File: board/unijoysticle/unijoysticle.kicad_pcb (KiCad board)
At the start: 2 copper layers, 57.9 x 52.6 mm, 10 parts, among them J1 DB9_Female_MountingHoles, J2 DB9_Female_MountingHoles, J3 Barrel_Jack_MountingPin, SW1 SW_SPDT, U1 4066, U2 4066, U4 4066, U5 4066

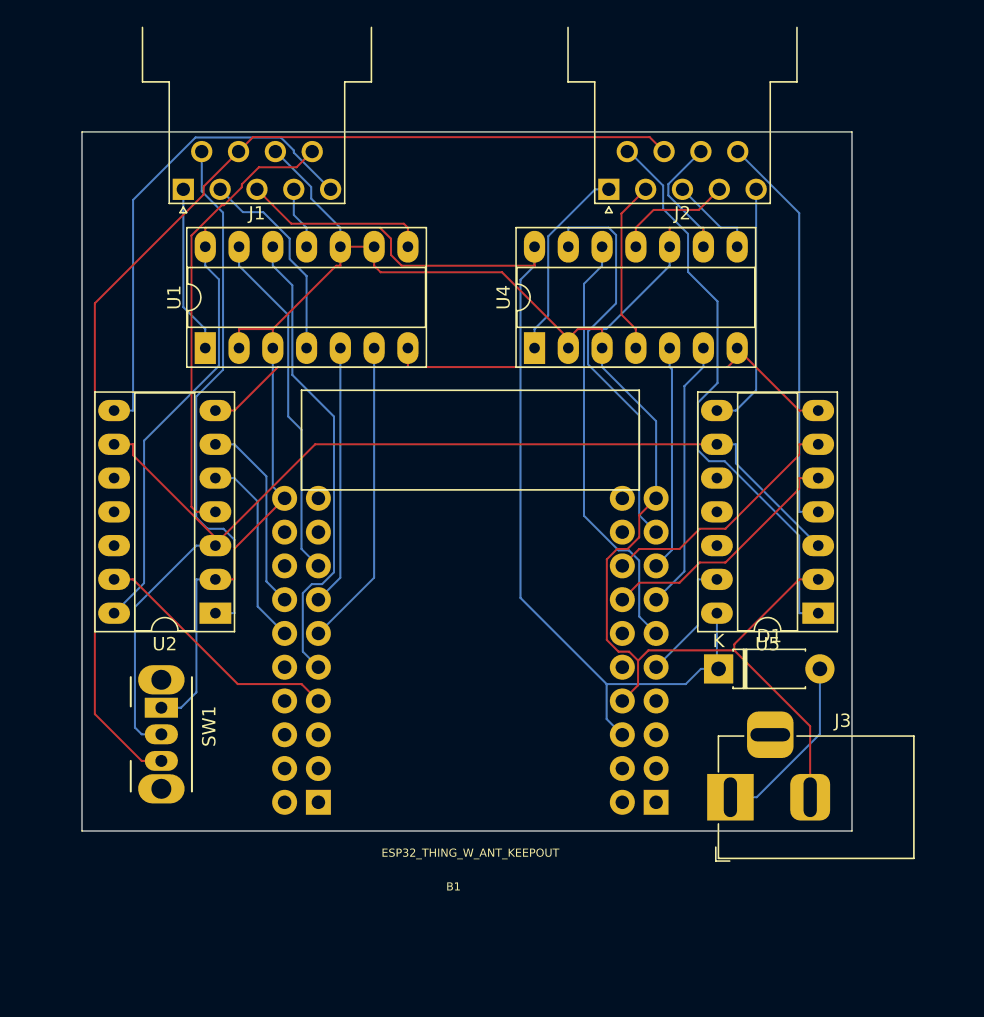
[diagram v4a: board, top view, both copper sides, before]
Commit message: board: using new db9 female to avoid errors.
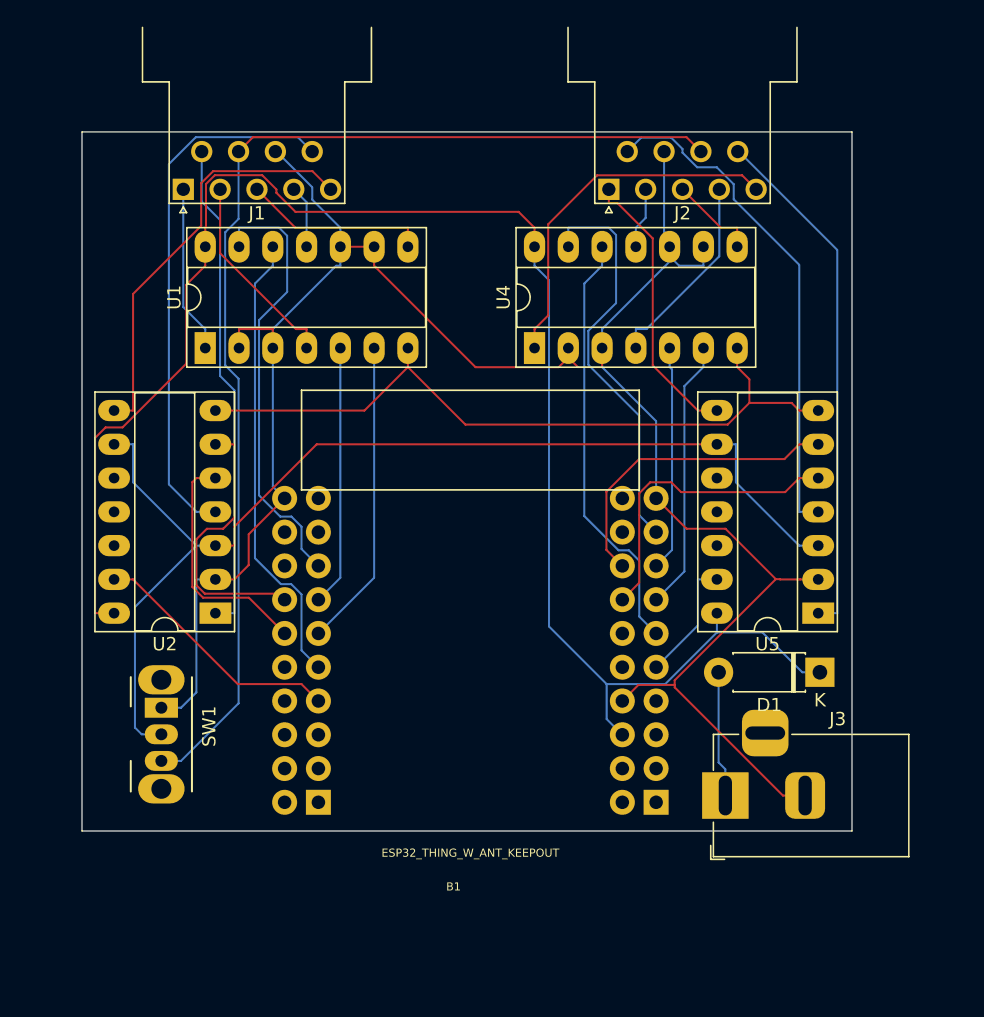
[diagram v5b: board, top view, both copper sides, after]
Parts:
- J1, J2: value DB9_Female_MountingHoles -> DB9_Female
- J3: value Barrel_Jack_MountingPin -> Barrel_Jack
- moved D1 7.62 mm to (168.7, 115.6), turned to 180 degrees
- moved J3 0.40 mm to (161.5, 124.8)
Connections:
- J2 pad 1: J2UP -> J2POTY
- J2 pad 2: J2DOWN -> J2RIGHT
- J2 pad 4: J2RIGHT -> J2DOWN
- J2 pad 5: J2POTY -> J2UP
- J2 pad 6: J2FIRE -> J2POTX
- J2 pad 7: J1POWER -> GND
- J2 pad 8: GND -> J1POWER
- J2 pad 9: J2POTX -> J2FIRE
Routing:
- net J2UP: track 14.9 -> 27.3 mm
- net Vdd: track 114.4 -> 125.9 mm
- net J2POTX: track 30.4 -> 38.2 mm
- net GPIO_J1UP: track 26.5 -> 33.3 mm
- net GPIO_J1POTY: track 14.7 -> 21.0 mm
- net J1POTX: track 34.2 -> 40.5 mm
- net GND: track 169.3 -> 163.2 mm
- net Vss: track 50.8 -> 55.3 mm
- net GPIO_J2POTY: track 19.0 -> 23.5 mm
- net J1POTY: track 35.8 -> 31.3 mm
- net J2RIGHT: track 8.90 -> 4.62 mm
- net J2FIRE: track 43.5 -> 39.3 mm
- net Net-(D1-Pad2): track 13.6 -> 9.48 mm
- net GPIO_J2POTX: track 19.0 -> 23.1 mm
- net GPIO_J1POTX: track 14.7 -> 18.1 mm
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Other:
- rule via_min_drill: 0.254 -> 0.3302
- rule via_min_size: 0.508 -> 0.6858

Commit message: board: add logo in back silkscreen
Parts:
- added G***: LOGO, Parts:unijoysticle_logo, B.Cu at (141.5, 106.4)
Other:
- board text added: "Unijoysticle 2 v0.0.1 http://retro.moe"

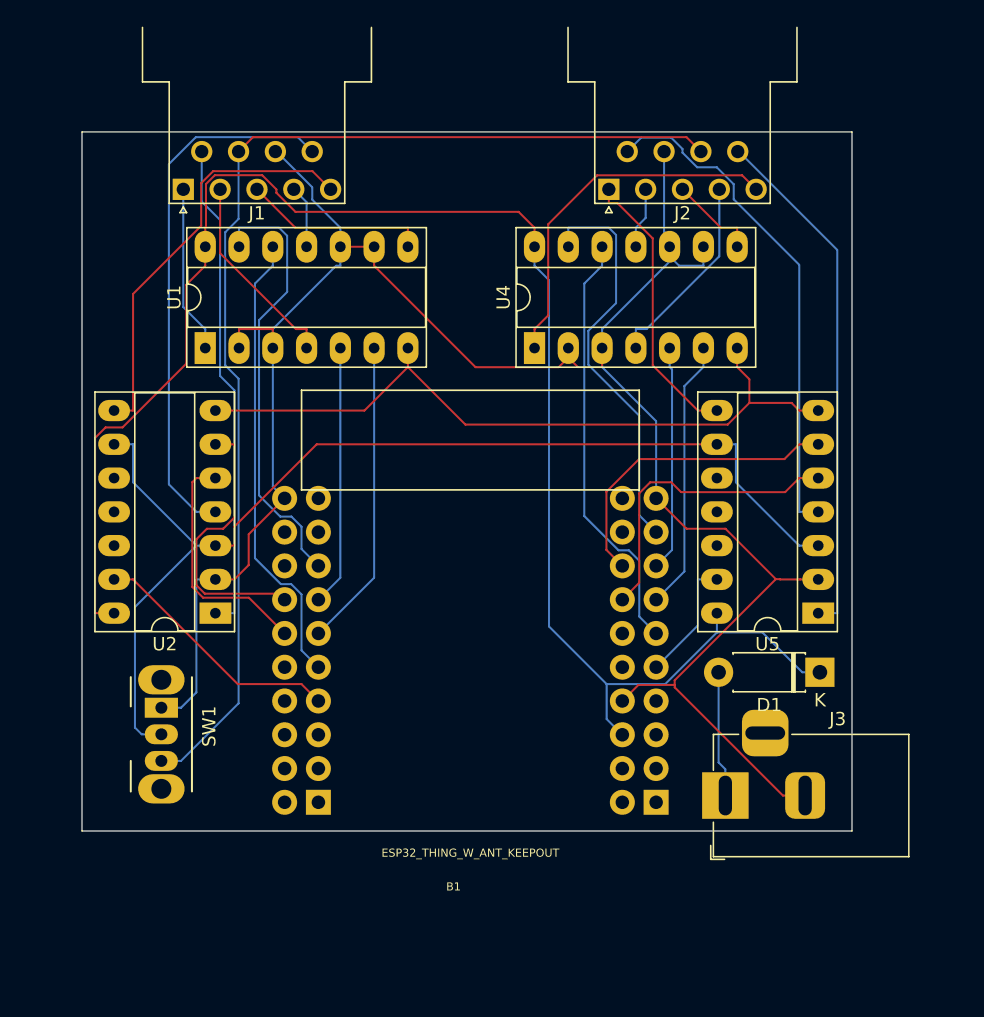
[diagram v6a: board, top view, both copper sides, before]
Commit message: board: autorouting ok. j1 & j2 connected correctly
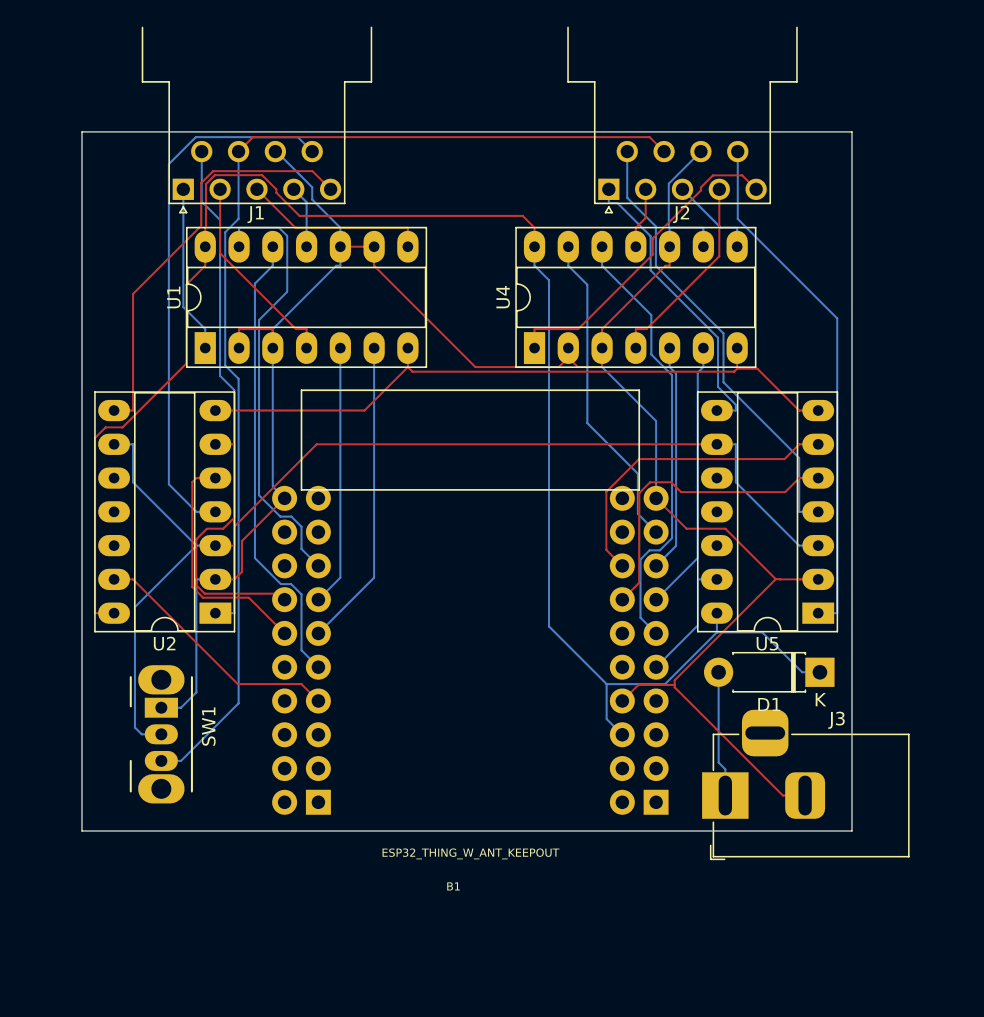
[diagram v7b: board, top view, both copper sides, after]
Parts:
- removed G***: LOGO, Parts:unijoysticle_logo
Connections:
- B1 pad 2: VDD -> Vdd
- D1 pad 1: VDD -> Vdd
- J2 pad 7: GND -> J1POWER
- J2 pad 8: J1POWER -> GND
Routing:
- net GPIO_J2UP: track 30.6 -> 24.2 mm
- net J2POTX: track 38.2 -> 33.9 mm
- net Vss: track 55.3 -> 51.2 mm
- net J2UP: track 27.3 -> 24.2 mm
- net J1POWER: track 85.6 -> 82.8 mm
- net J2POTY: track 21.2 -> 22.4 mm
- net GPIO_J2RIGHT: track 32.3 -> 33.2 mm
- net GND: track 163.2 -> 164.0 mm

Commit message: board: logo re-added, c64/amiga legends and more
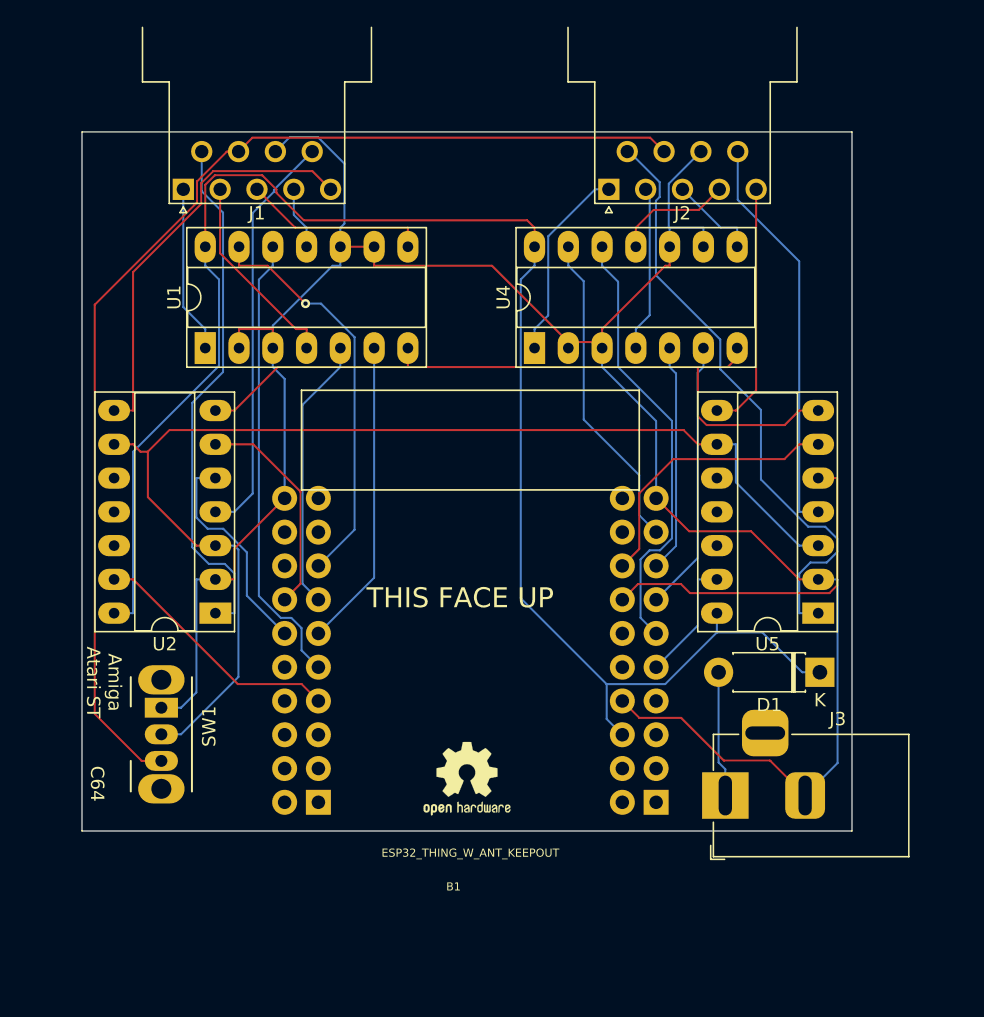
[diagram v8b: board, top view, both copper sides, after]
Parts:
- added G***: LOGO, Parts:unijoysticle_logo, B.Cu at (141.5, 105.0)
- added REF**: OSHW-Logo2_7.3x6mm_SilkScreen, Symbol:OSHW-Logo2_7.3x6mm_SilkScreen, F.Cu at (142.1, 123.6)
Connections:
- J2 pad 1: J2POTY -> J2UP
- J2 pad 2: J2RIGHT -> J2DOWN
- J2 pad 4: J2DOWN -> J2RIGHT
- J2 pad 5: J2UP -> J2POTY
- J2 pad 6: J2POTX -> J2FIRE
- J2 pad 9: J2FIRE -> J2POTX
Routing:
- net J1POTX: track 40.5 -> 31.0 mm
- net J2UP: track 24.2 -> 14.9 mm
- net GND: track 164.0 -> 171.2 mm
- net J2FIRE: track 39.2 -> 45.7 mm
- net Vss: track 51.2 -> 56.5 mm
- net GPIO_J1POTY: track 21.0 -> 16.5 mm
- net J2RIGHT: track 4.62 -> 8.90 mm
- net J1POWER: track 82.8 -> 86.6 mm
- net POWER_OR_GND: track 84.4 -> 88.2 mm
- net J2POTY: track 22.4 -> 18.7 mm
- net GPIO_J2POTX: track 23.1 -> 26.7 mm
- net J2POTX: track 33.9 -> 30.4 mm
- net GPIO_J1UP: track 33.3 -> 30.7 mm, vias 0 -> 1
- net J1FIRE: track 37.2 -> 39.8 mm
- net J2DOWN: track 15.0 -> 12.5 mm
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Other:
- board text added: "Amiga Atari ST"
- board text added: "C64"
- board text added: "THIS FACE UP"
